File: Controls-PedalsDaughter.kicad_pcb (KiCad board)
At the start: 2 copper layers, 49.2 x 71.5 mm, 54 parts, among them J1 Brake Pos. Sensor, J2 Accel Pos. Sensor, J3 PeripheralCANConnector, J4 Conn_01x02, J5 PeripheralCANConnector, U1 RI3-1205S, U2 PeripheralSOM, U3 TLV9301xDCK, U4 TLV70130DBVR, U5 AMC1300BDWV, U6 TLV9301xDCK

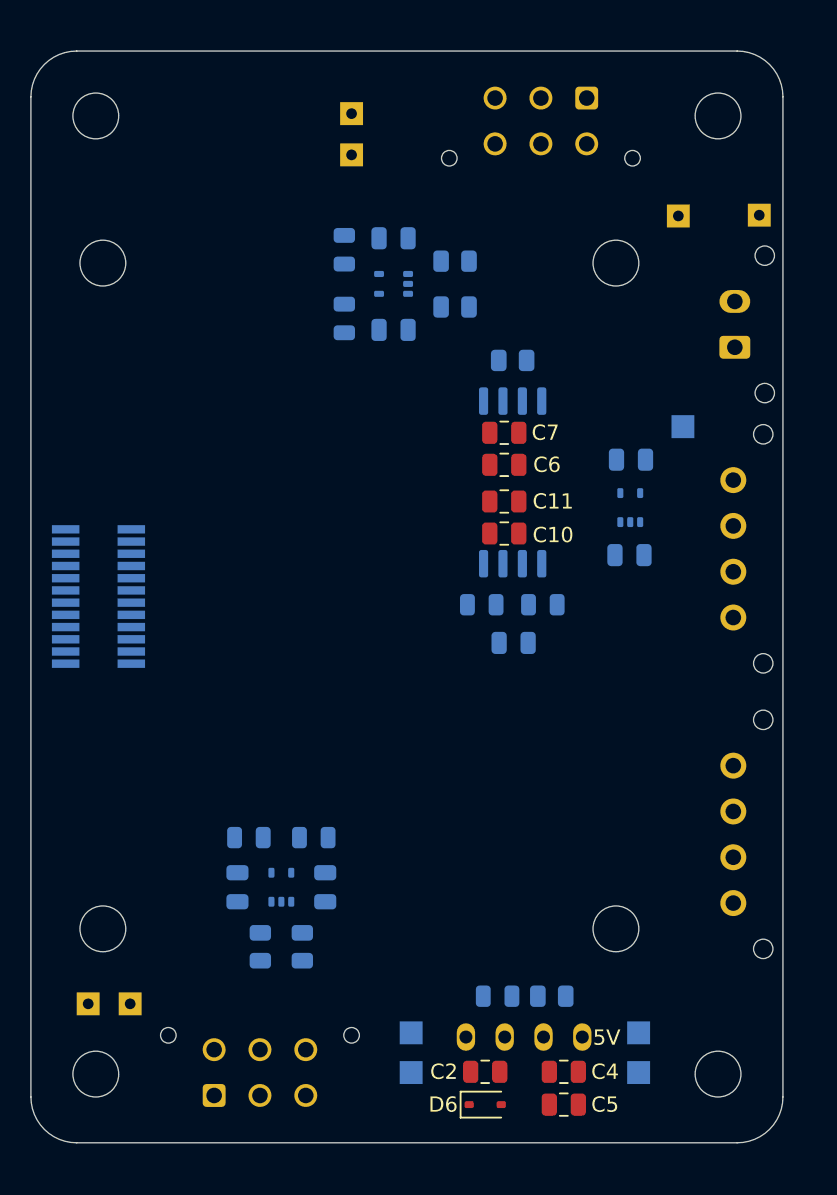
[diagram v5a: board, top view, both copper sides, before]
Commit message: added space for latching
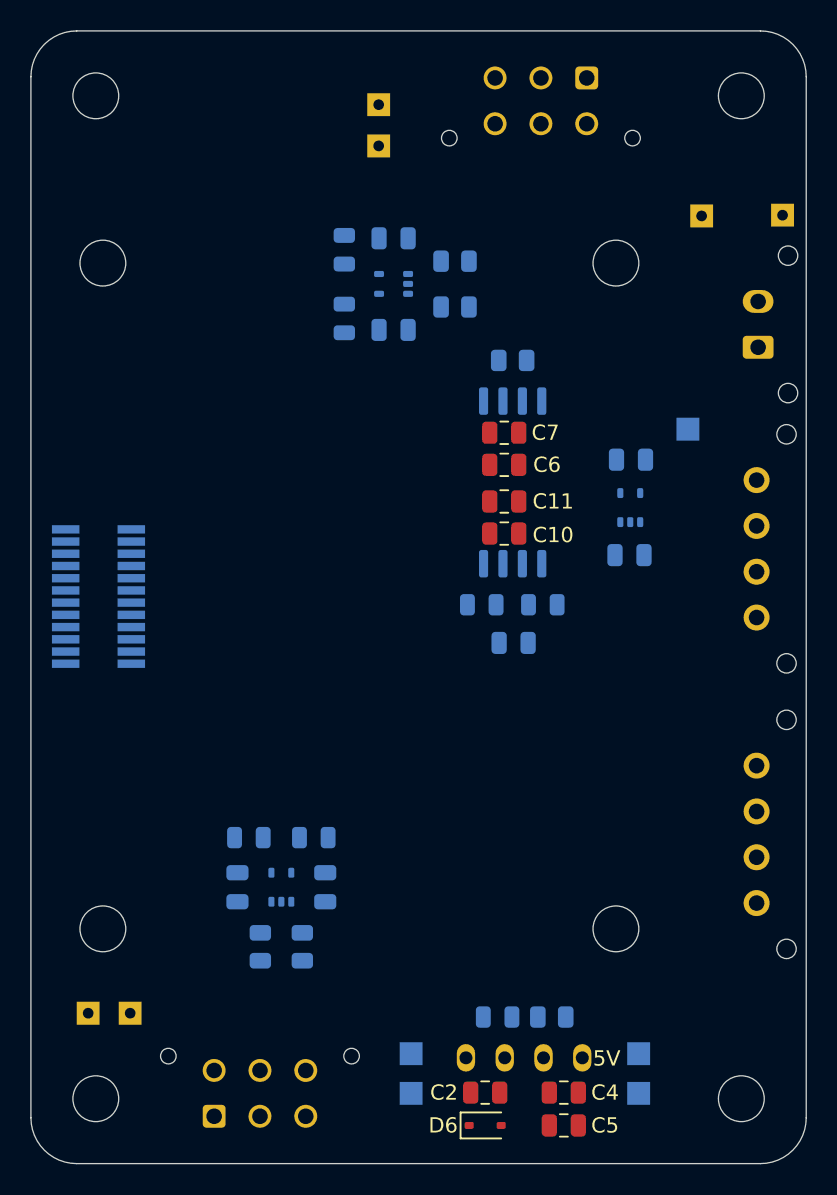
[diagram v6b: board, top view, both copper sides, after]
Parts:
- moved ? 2.22 mm to (172.2, 132.8)
- moved ? 2.02 mm to (172.2, 67.2)
- moved Brake_TP1 1.87 mm to (145.2, 67.8)
- moved Brake_Raw1 1.87 mm to (145.2, 70.5)
- moved ? 1.61 mm to (130.0, 132.8)
- moved Brake_Fl_Sn1 1.53 mm to (166.4, 75.0)
- moved J3 1.53 mm to (170.0, 120.0)
- moved J4 1.53 mm to (170.1, 83.6)
- moved J5 1.53 mm to (170.0, 101.3)
- moved Brake_Fl_Sn_Raw1 1.52 mm to (171.7, 75.0)
- moved +12V1 1.36 mm to (147.4, 129.9)
- moved +5V1 1.36 mm to (162.3, 129.9)
- moved GND1 1.36 mm to (162.3, 132.5)
- moved GNDPWR1 1.36 mm to (147.4, 132.5)
- moved J2 1.36 mm to (134.5, 134.0)
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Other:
- board size 49.2 x 71.5 mm -> 50.8 x 74.2 mm

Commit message: routed for the first time ever
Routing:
- net +3V3: track 0.00 -> 76.4 mm, vias 0 -> 5
- net /CAN_H: track 0.00 -> 63.2 mm, vias 0 -> 1
- net /CAN_L: track 0.00 -> 62.7 mm, vias 0 -> 2
- net /Brake_Fl: track 0.00 -> 61.8 mm, vias 0 -> 1
- net /Brake_Pot: track 0.00 -> 56.2 mm, vias 0 -> 2
- net +12V: track 0.00 -> 55.2 mm, vias 0 -> 5
- net GNDPWR: track 0.00 -> 51.9 mm, vias 0 -> 5
- net /Accel: track 0.00 -> 41.7 mm
- net /Brake Fluid Sensor/INP: track 0.00 -> 28.4 mm
- net +3V3PWR: track 0.00 -> 20.6 mm, vias 0 -> 2
- net Net-(U3-+): track 0.00 -> 19.8 mm
- net Net-(U6-+): track 0.00 -> 14.8 mm
- net Net-(J1-Pin_5): track 0.00 -> 11.0 mm
- net Net-(J2-Pin_5): track 0.00 -> 7.20 mm
- net GND: track 0.00 -> 6.26 mm, vias 0 -> 6
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- added copper zone on F.Cu, net +12V
- added copper zone on F.Cu, net +5V
- added copper zone on B.Cu, net GND
- added copper zone on B.Cu, net GNDPWR

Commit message: Ravi <3
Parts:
- C4: moved to B.Cu
- H1, H2, H3: renamed from ?; value (none) -> MountingHole
- R3: moved to F.Cu
- moved R3 62.1 mm to (133.2, 70.0), turned to 0 degrees
- moved PWR_LED 60.3 mm to (135.0, 70.0), turned to 180 degrees
- moved C4 7.85 mm to (155.6, 124.8)
- moved C5 7.43 mm to (158.0, 127.2)
- moved +5V 1.90 mm to (162.3, 128.0)
- moved GND 1.90 mm to (162.3, 130.6)
- moved C2 1.19 mm to (151.2, 133.1)
- moved D6 1.19 mm to (151.2, 135.2)
- moved J1 0.40 mm to (158.9, 66.4)
- moved J2 0.40 mm to (134.5, 133.6)
- moved J4 0.30 mm to (169.8, 83.6)
- moved J5 0.26 mm to (169.8, 101.2)
- moved J3 0.25 mm to (169.8, 120.0)
- moved R1 0.10 mm to (154.0, 84.4)
- moved U1 0.10 mm to (154.8, 130.1)
- renumbered +12V1 to +12V, +5V1 to +5V, Accel_Raw1 to Accel_Raw, Accel_TP1 to Accel_TP, Brake_Fl_Sn1 to Brake_Fl_Sn, Brake_Fl_Sn_Raw1 to Brake_Fl_Sn_Raw, Brake_Raw1 to Brake_Raw, Brake_TP1 to Brake_TP, GND1 to GND, GNDPWR1 to GNDPWR, D7 to PWR_LED, TP_3V3PWR1 to TP_3V3PWR
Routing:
- net +12V: track 55.2 -> 2.27 mm, vias 5 -> 3
- net GNDPWR: track 51.9 -> 2.19 mm, vias 5 -> 3
- net GND: track 6.26 -> 0.00 mm, vias 6 -> 3
- net /Brake_Fl: track 61.8 -> 66.8 mm, vias 1 -> 3
- net +5V: track 0.00 -> 4.56 mm, vias 6 -> 4
- net /CAN_H: track 63.2 -> 66.8 mm, vias 1 -> 3
- net Net-(D7-A): track 1.70 -> 0.00 mm, vias 0 -> 1
- net /CAN_L: track 62.7 -> 64.0 mm
- net /Brake_Pot: track 56.2 -> 56.7 mm
- net +3V3: track 76.4 -> 76.9 mm, vias 5 -> 7
- net /Accel: track 41.7 -> 42.0 mm, vias 0 -> 2
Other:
- board text added: "12V"
- board text added: "Accel"
- board text added: "Brake"
- board text added: "CAN"
- board text added: "FL_SN"
